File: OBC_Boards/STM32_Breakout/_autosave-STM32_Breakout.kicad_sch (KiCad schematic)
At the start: 106 parts, among them J1 Conn_02x20_Odd_Even, J2 1050171001, J3 1050171001, J4 105017-1001, J5 SSQ-105-03-T-D, J6 SSQ-105-03-T-D, J7 ST1W008S4ER1500-MicroSDConnec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, J8 105017-1001, Q1 Q_PMOS_DGS, U1 MCP7940NT-I_MS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

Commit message: Fix all clearance, silkscreen and trace errors. Partially fixed 3.3V traces
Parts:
- gave numbers to parts that had none: 1
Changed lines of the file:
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@@
   (symbol (lib_id "STM32_Breakout-rescue:R0603-OBC_Libary") (at 486.41 38.1 180) (unit 1)
     (in_bom yes) (on_board yes)
-    (property "Reference" "R?" (id 0) (at 487.68 40.64 0)
+    (property "Reference" "R23" (id 0) (at 487.68 40.64 0)
       (effects (font (size 1.27 1.27)) (justify left))
     )
@@
       (reference "R22") (unit 1) (value "10k") (footprint "RESC1607X60N")
     )
+    (path "/4d90e891-d752-480f-a4d6-707889dcf29b"
+      (reference "R23") (unit 1) (value "0R") (footprint "RESC1607X60N")
+    )
     (path "/00000000-0000-0000-0000-000061ca0288"
       (reference "R24") (unit 1) (value "10k +-1%") (footprint "RESC1607X60N")
@@
       (reference "R32") (unit 1) (value "0R") (footprint "RESC1607X60N")
     )
-    (path "/4d90e891-d752-480f-a4d6-707889dcf29b"
-      (reference "R?") (unit 1) (value "0R") (footprint "RESC1607X60N")
-    )
     (path "/7f6779b3-84f5-4c42-a9d1-fb8c88a13301"

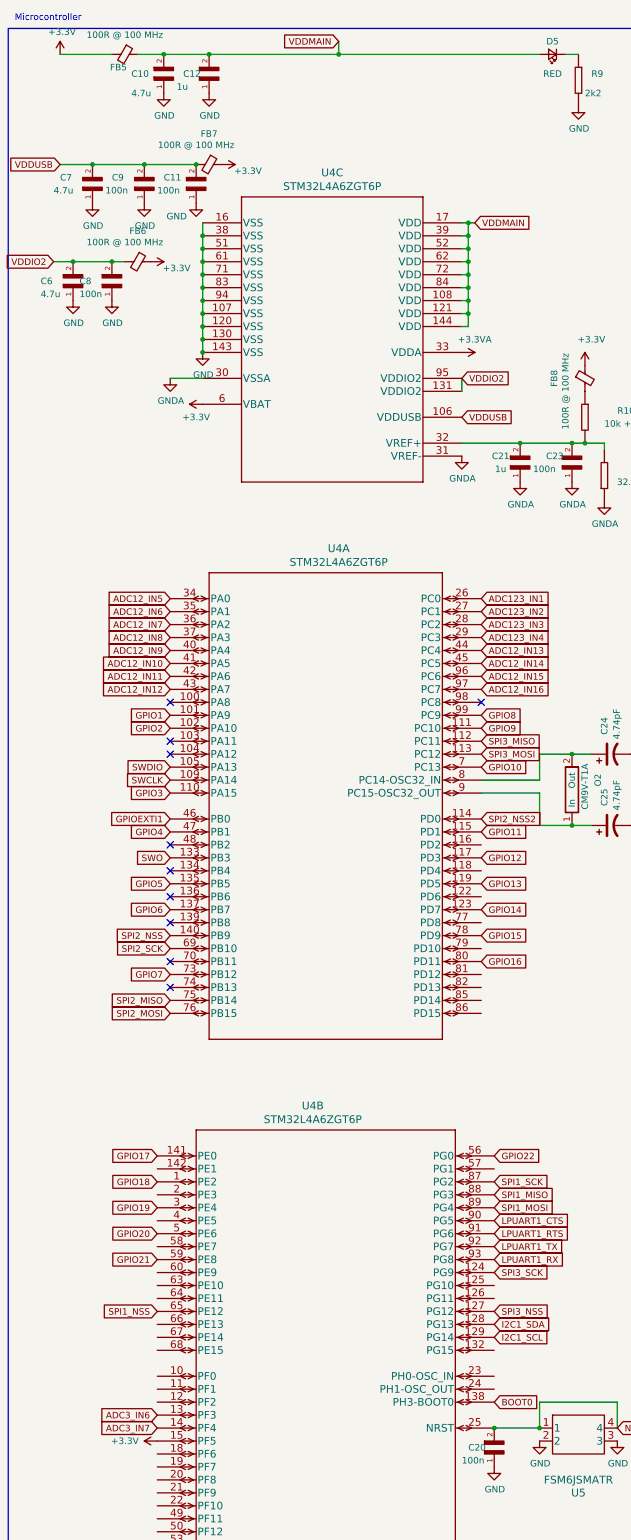
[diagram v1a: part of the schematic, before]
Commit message: Continue to work on power distribution within the board
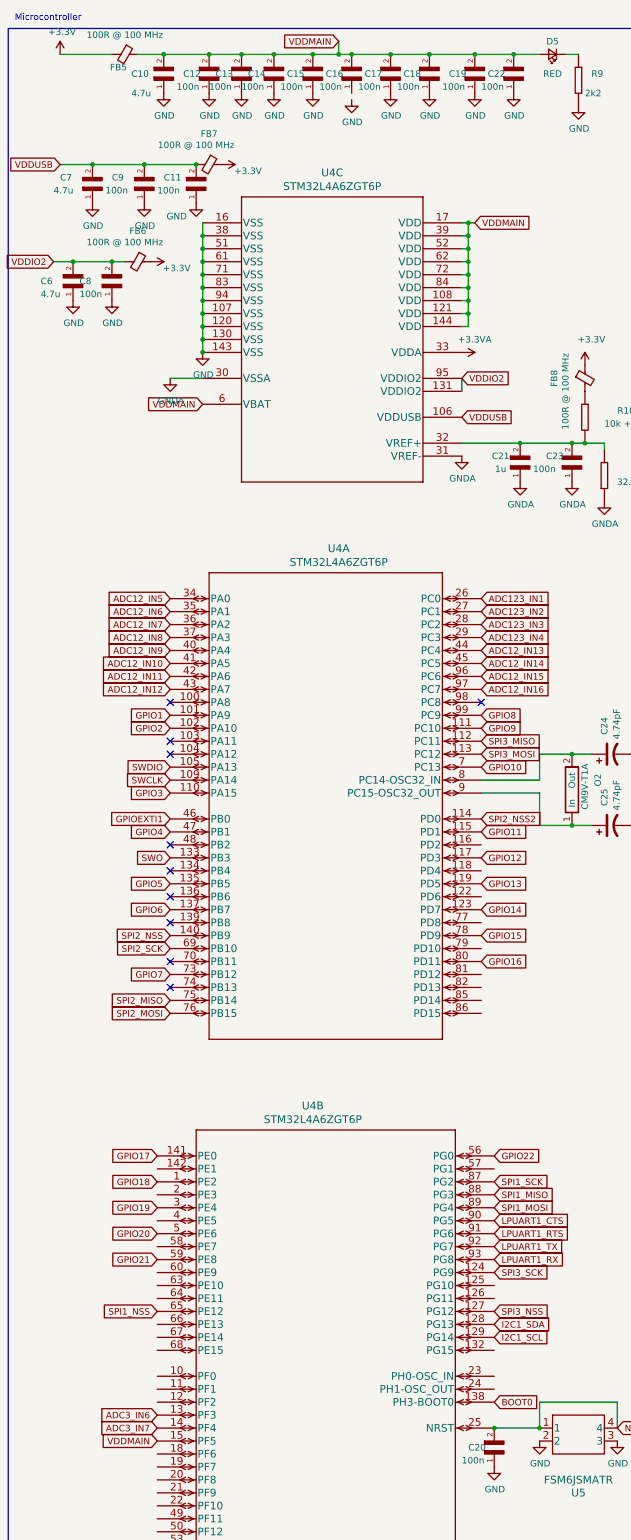
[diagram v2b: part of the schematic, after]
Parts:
- added C13, C14, C15, C16, C17, C18, C19, C22: 100n, CAPC1608X90, symbol STM32_Breakout-rescue:CC0603MRX5R5BB475-CC0603MRX5R5BB475
- C12: value 1u -> 100n
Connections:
- net +3V3: no longer U4.15 (PF5), U4.6 (VBAT)
- net GND: now also C13.1, C14.1, C15.1, C17.1, C18.1, C19.1, C22.1
- net VDDMAIN: now also U4.15 (PF5), U4.6 (VBAT), C13.2, C14.2, C15.2, C16.2, C17.2, C18.2, C19.2, C22.2
